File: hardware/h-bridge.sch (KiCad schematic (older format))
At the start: 46 parts, among them P3 CONN_01X02, Q3 IRFP4468, Q4 IRFP4468, Q5 IRFP4468, Q6 IRFP4468, Q7 IRFP4468, Q8 IRFP4468, U12 Si8660, U13 MIC4127, U14 LM5102, U15 LM5102

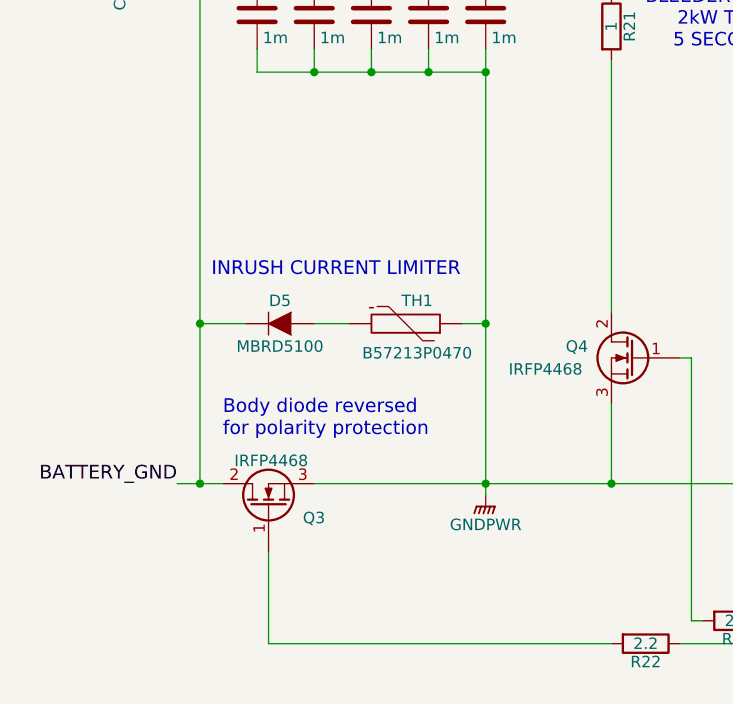
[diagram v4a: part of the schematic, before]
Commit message: Finish MCU HW draft 1; adjust sensors for 3v ref
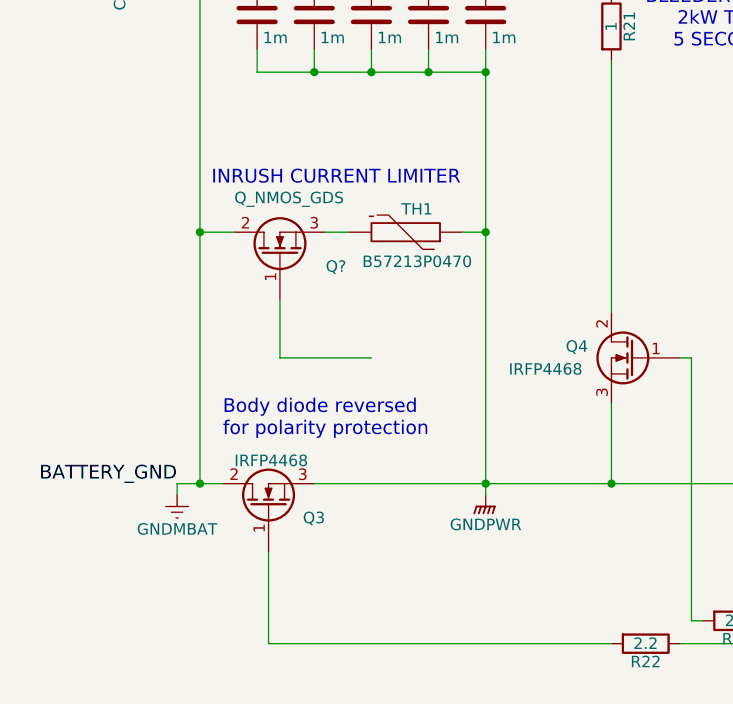
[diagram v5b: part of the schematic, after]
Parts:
- removed D5: MBRD5100, TO_SOT_Packages_SMD:TO-263-3Lead, symbol D
- added Q?: Q_NMOS_GDS, symbol Q_NMOS_GDS
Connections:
- net at TH1.2: now also Q?.3 (S)
- net BATTERY_GND renamed GNDMBAT
- net GNDMBAT: now also Q?.2 (D)
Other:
- moved on the sheet: TH1
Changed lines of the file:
@@
 L THERMISTOR TH1
 U 1 1 5986B315
-P 2550 3100
-F 0 "TH1" V 2650 3150 50  0000 C CNN
-F 1 "B57213P0470" V 2450 3150 50  0000 C BNN
-F 2 "Resistors_ThroughHole:Resistor_Vertical_RM7.5mm" H 2550 3100 50  0001 C CNN
-F 3 "" H 2550 3100 50  0000 C CNN
-	1    2550 3100
+P 2550 2700
+F 0 "TH1" V 2650 2750 50  0000 C CNN
+F 1 "B57213P0470" V 2450 2750 50  0000 C BNN
+F 2 "Resistors_ThroughHole:Resistor_Vertical_RM7.5mm" H 2550 2700 50  0001 C CNN
+F 3 "" H 2550 2700 50  0000 C CNN
+	1    2550 2700
 	0    1    -1   0
 $EndComp
@@
 Text Label 4300 6450 0    60   ~ 0
 PWM4_GD
-$Comp
-L D D5
-U 1 1 599E1390
-P 2000 3100
-F 0 "D5" H 2000 3200 50  0000 C CNN
-F 1 "MBRD5100" H 2000 3000 50  0000 C CNN
-F 2 "TO_SOT_Packages_SMD:TO-263-3Lead" H 2000 3100 50  0001 C CNN
-F 3 "" H 2000 3100 50  0000 C CNN
-	1    2000 3100
-	1    0    0    -1
-$EndComp
 Text Notes 1750 3600 0    60   ~ 0
 Body diode reversed\nfor polarity protection
@@
 	-1   0    0    -1
 $EndComp
+$Comp
+L +12V_ISO #PWR071
+U 1 1 59A0BCFD
+P 5850 4150
+F 0 "#PWR071" H 5850 4000 50  0001 C CNN
+F 1 "+12V_ISO" H 5850 4290 50  0000 C CNN
+F 2 "" H 5850 4150 50  0000 C CNN
+F 3 "" H 5850 4150 50  0000 C CNN
+	1    5850 4150
+	1    0    0    -1
+$EndComp
+$Comp
+L C_Small C42
+U 1 1 59A0C68A
+P 5850 4450
+F 0 "C42" H 5860 4520 50  0000 L CNN
+F 1 "100n" H 5860 4370 50  0000 L CNN
+F 2 "Capacitors_SMD:C_0603" H 5850 4450 50  0001 C CNN
+F 3 "" H 5850 4450 50  0000 C CNN
+	1    5850 4450
+	1    0    0    -1
+$EndComp
+Text Label 5150 4400 0    60   ~ 0
+VBUS_DIS_GD
+Text Label 5150 4500 0    60   ~ 0
+VBUS_EN_GD
+$Comp
+L R R22
+U 1 1 59A124D4
+P 3600 4500
+F 0 "R22" V 3680 4500 50  0000 C CNN
+F 1 "2.2" V 3600 4500 50  0000 C CNN
+F 2 "Resistors_SMD:R_0603" V 3530 4500 50  0001 C CNN
+F 3 "" H 3600 4500 50  0000 C CNN
+	1    3600 4500
+	0    1    1    0
+$EndComp
+$Comp
+L R R23
+U 1 1 59A12613
+P 4000 4400
+F 0 "R23" V 4080 4400 50  0000 C CNN
+F 1 "2.2" V 4000 4400 50  0000 C CNN
+F 2 "Resistors_SMD:R_0603" V 3930 4400 50  0001 C CNN
+F 3 "" H 4000 4400 50  0000 C CNN
+	1    4000 4400
+	0    1    1    0
+$EndComp
+$Comp
+L GNDPWR #PWR072
+U 1 1 59A194F2
+P 5150 3850
+F 0 "#PWR072" H 5150 3650 50  0001 C CNN
+F 1 "GNDPWR" H 5150 3720 50  0000 C CNN
+F 2 "" H 5150 3800 50  0000 C CNN
+F 3 "" H 5150 3800 50  0000 C CNN
+	1    5150 3850
+	1    0    0    -1
+$EndComp
+$Comp
+L GNDPWR #PWR073
+U 1 1 59A199E4
+P 9750 3850
+F 0 "#PWR073" H 9750 3650 50  0001 C CNN
+F 1 "GNDPWR" H 9750 3720 50  0000 C CNN
+F 2 "" H 9750 3800 50  0000 C CNN
+F 3 "" H 9750 3800 50  0000 C CNN
+	1    9750 3850
+	1    0    0    -1
+$EndComp
+$Comp
+L Si8660 U12
+U 1 1 59A1E1D2
+P 3650 6400
+F 0 "U12" H 3650 5850 60  0000 C CNN
+F 1 "Si8660" H 3650 6950 60  0000 C CNN
+F 2 "Housings_SOIC:SOIC-16_3.9x9.9mm_Pitch1.27mm" H 3650 6450 60  0001 C CNN
+F 3 "" H 3650 6450 60  0000 C CNN
+	1    3650 6400
+	1    0    0    -1
+$EndComp
+$Comp
+L GND #PWR074
+U 1 1 59A2238F
+P 3050 7000
+F 0 "#PWR074" H 3050 6750 50  0001 C CNN
+F 1 "GND" H 3050 6850 50  0000 C CNN
+F 2 "" H 3050 7000 50  0000 C CNN
+F 3 "" H 3050 7000 50  0000 C CNN
+	1    3050 7000
+	1    0    0    -1
+$EndComp
+$Comp
+L GNDPWR #PWR075
+U 1 1 59A24543
+P 4250 7100
+F 0 "#PWR075" H 4250 6900 50  0001 C CNN
+F 1 "GNDPWR" H 4250 6970 50  0000 C CNN
+F 2 "" H 4250 7050 50  0000 C CNN
+F 3 "" H 4250 7050 50  0000 C CNN
+	1    4250 7100
+	1    0    0    -1
+$EndComp
+$Comp
+L R R30
+U 1 1 59A2EED2
+P 5700 6800
+F 0 "R30" V 5780 6800 50  0000 C CNN
+F 1 "10k" V 5700 6800 50  0000 C CNN
+F 2 "Resistors_SMD:R_0603" V 5630 6800 50  0001 C CNN
+F 3 "" H 5700 6800 50  0000 C CNN
+	1    5700 6800
+	1    0    0    -1
+$EndComp
+$Comp
+L R R31
+U 1 1 59A2EED8
+P 5900 6800
+F 0 "R31" V 5980 6800 50  0000 C CNN
+F 1 "10k" V 5900 6800 50  0000 C CNN
+F 2 "Resistors_SMD:R_0603" V 5830 6800 50  0001 C CNN
+F 3 "" H 5900 6800 50  0000 C CNN
+	1    5900 6800
+	1    0    0    -1
+$EndComp
+Text Label 4300 6550 0    60   ~ 0
+VBUS_DIS_GD
+Text Label 4300 6650 0    60   ~ 0
+VBUS_EN_GD
+Text Notes 1700 2500 0    60   ~ 0
+INRUSH CURRENT LIMITER
+Text HLabel 7300 2950 3    60   BiDi ~ 0
+I_SENSE+
+Text HLabel 7550 2950 3    60   BiDi ~ 0
+I_SENSE-
+Text HLabel 8300 1450 2    60   Output ~ 0
+VBUS
+$Comp
+L GNDMBAT #PWR?
+U 1 1 59C09326
+P 1550 3850
+F 0 "#PWR?" H 1550 3600 50  0001 C CNN
+F 1 "GNDMBAT" H 1550 3700 50  0000 C CNN
+F 2 "" H 1550 3850 50  0000 C CNN
+F 3 "" H 1550 3850 50  0000 C CNN
+	1    1550 3850
+	1    0    0    -1
+$EndComp
 Wire Wire Line
 	6700 2650 6700 3300
@@
 Wire Wire Line
 	2150 1450 2150 1600
-Wire Wire Line
-	2900 1900 2900 3850
 Connection ~ 2900 2000
 Wire Wire Line
@@
 Wire Wire Line
 	1900 2000 2900 2000
-Wire Wire Line
-	2800 3100 2900 3100
-Connection ~ 2900 3100
-Wire Wire Line
-	1650 3100 1850 3100
-Connection ~ 1650 3100
+Connection ~ 1650 2700
 Connection ~ 2900 3800
 Wire Wire Line
@@
 	4900 6950 4900 7000
 Connection ~ 4900 7000
-Wire Wire Line
-	2150 3100 2300 3100
 Connection ~ 3450 3800
 Connection ~ 3450 1450
 Wire Wire Line
 	5100 4650 6050 4650
-$Comp
-L +12V_ISO #PWR071
-U 1 1 59A0BCFD
-P 5850 4150
-F 0 "#PWR071" H 5850 4000 50  0001 C CNN
-F 1 "+12V_ISO" H 5850 4290 50  0000 C CNN
-F 2 "" H 5850 4150 50  0000 C CNN
-F 3 "" H 5850 4150 50  0000 C CNN
-	1    5850 4150
-	1    0    0    -1
-$EndComp
 Wire Wire Line
 	5100 4250 5850 4250
-$Comp
-L C_Small C42
-U 1 1 59A0C68A
-P 5850 4450
-F 0 "C42" H 5860 4520 50  0000 L CNN
-F 1 "100n" H 5860 4370 50  0000 L CNN
-F 2 "Capacitors_SMD:C_0603" H 5850 4450 50  0001 C CNN
-F 3 "" H 5850 4450 50  0000 C CNN
-	1    5850 4450
-	1    0    0    -1
-$EndComp
 Wire Wire Line
 	5850 4150 5850 4350
 Wire Wire Line
 	5850 4550 5850 4650
-Text Label 5150 4400 0    60   ~ 0
-VBUS_DIS_GD
 Wire Wire Line
 	5100 4400 5150 4400
 Wire Wire Line
 	5100 4500 5150 4500
-Text Label 5150 4500 0    60   ~ 0
-VBUS_EN_GD
 Connection ~ 5850 4650
 Wire Wire Line
@@
 Wire Wire Line
 	1950 4100 1950 4500
-$Comp
-L R R22
-U 1 1 59A124D4
-P 3600 4500
-F 0 "R22" V 3680 4500 50  0000 C CNN
-F 1 "2.2" V 3600 4500 50  0000 C CNN
-F 2 "Resistors_SMD:R_0603" V 3530 4500 50  0001 C CNN
-F 3 "" H 3600 4500 50  0000 C CNN
-	1    3600 4500
-	0    1    1    0
-$EndComp
-$Comp
-L R R23
-U 1 1 59A12613
-P 4000 4400
-F 0 "R23" V 4080 4400 50  0000 C CNN
-F 1 "2.2" V 4000 4400 50  0000 C CNN
-F 2 "Resistors_SMD:R_0603" V 3930 4400 50  0001 C CNN
-F 3 "" H 4000 4400 50  0000 C CNN
-	1    4000 4400
-	0    1    1    0
-$EndComp
 Connection ~ 6050 3800
 Wire Wire Line
@@
 Wire Wire Line
 	1950 4500 3450 4500
-$Comp
-L GNDPWR #PWR072
-U 1 1 59A194F2
-P 5150 3850
-F 0 "#PWR072" H 5150 3650 50  0001 C CNN
-F 1 "GNDPWR" H 5150 3720 50  0000 C CNN
-F 2 "" H 5150 3800 50  0000 C CNN
-F 3 "" H 5150 3800 50  0000 C CNN
-	1    5150 3850
-	1    0    0    -1
-$EndComp
-$Comp
-L GNDPWR #PWR073
-U 1 1 59A199E4
-P 9750 3850
-F 0 "#PWR073" H 9750 3650 50  0001 C CNN
-F 1 "GNDPWR" H 9750 3720 50  0000 C CNN
-F 2 "" H 9750 3800 50  0000 C CNN
-F 3 "" H 9750 3800 50  0000 C CNN
-	1    9750 3850
-	1    0    0    -1
-$EndComp
 Connection ~ 5850 4250
-$Comp
-L Si8660 U12
-U 1 1 59A1E1D2
-P 3650 6400
-F 0 "U12" H 3650 5850 60  0000 C CNN
-F 1 "Si8660" H 3650 6950 60  0000 C CNN
-F 2 "Housings_SOIC:SOIC-16_3.9x9.9mm_Pitch1.27mm" H 3650 6450 60  0001 C CNN
-F 3 "" H 3650 6450 60  0000 C CNN
-	1    3650 6400
-	1    0    0    -1
-$EndComp
-$Comp
-L GND #PWR074
-U 1 1 59A2238F
-P 3050 7000
-F 0 "#PWR074" H 3050 6750 50  0001 C CNN
-F 1 "GND" H 3050 6850 50  0000 C CNN
-F 2 "" H 3050 7000 50  0000 C CNN
-F 3 "" H 3050 7000 50  0000 C CNN
-	1    3050 7000
-	1    0    0    -1
-$EndComp
-$Comp
-L GNDPWR #PWR075
-U 1 1 59A24543
-P 4250 7100
-F 0 "#PWR075" H 4250 6900 50  0001 C CNN
-F 1 "GNDPWR" H 4250 6970 50  0000 C CNN
-F 2 "" H 4250 7050 50  0000 C CNN
-F 3 "" H 4250 7050 50  0000 C CNN
-	1    4250 7100
-	1    0    0    -1
-$EndComp
 Wire Wire Line
 	3100 6850 3050 6850
@@
 Wire Wire Line
 	5300 6450 5300 6650
-$Comp
-L R R30
-U 1 1 59A2EED2
-P 5700 6800
-F 0 "R30" V 5780 6800 50  0000 C CNN
-F 1 "10k" V 5700 6800 50  0000 C CNN
-F 2 "Resistors_SMD:R_0603" V 5630 6800 50  0001 C CNN
-F 3 "" H 5700 6800 50  0000 C CNN
-	1    5700 6800
-	1    0    0    -1
-$EndComp
-$Comp
-L R R31
-U 1 1 59A2EED8
-P 5900 6800
-F 0 "R31" V 5980 6800 50  0000 C CNN
-F 1 "10k" V 5900 6800 50  0000 C CNN
-F 2 "Resistors_SMD:R_0603" V 5830 6800 50  0001 C CNN
-F 3 "" H 5900 6800 50  0000 C CNN
-	1    5900 6800
-	1    0    0    -1
-$EndComp
 Wire Wire Line
 	5700 7000 5700 6950
@@
 Wire Wire Line
 	5900 6150 5900 6650
-Text Label 4300 6550 0    60   ~ 0
-VBUS_DIS_GD
-Text Label 4300 6650 0    60   ~ 0
-VBUS_EN_GD
-Text Notes 1700 2900 0    60   ~ 0
-INRUSH CURRENT LIMITER
-Text HLabel 7300 2950 3    60   BiDi ~ 0
-I_SENSE+
-Text HLabel 7550 2950 3    60   BiDi ~ 0
-I_SENSE-
 Wire Wire Line
 	7300 2900 7300 2950
 Wire Wire Line
 	7550 2950 7550 2900
-Text HLabel 8300 1450 2    60   Output ~ 0
-VBUS
 Connection ~ 8200 1450
 Connection ~ 1900 1450
 Connection ~ 2150 1450
+Wire Wire Line
+	1550 3850 1550 3800
+Wire Wire Line
+	1650 2700 1800 2700
+Wire Wire Line
+	2200 2700 2300 2700
+Connection ~ 2900 2700
+Wire Wire Line
+	2900 2700 2800 2700
+Wire Wire Line
+	2900 1900 2900 3850
+$Comp
+L Q_NMOS_GDS Q?
+U 1 1 59C7B948
+P 2000 2800
+F 0 "Q?" V 1950 2600 50  0000 R CNN
+F 1 "Q_NMOS_GDS" V 2250 3000 50  0000 R CNN
+F 2 "" H 2200 2900 50  0000 C CNN
+F 3 "" H 2000 2800 50  0000 C CNN
+	1    2000 2800
+	0    -1   -1   0
+$EndComp
+Wire Wire Line
+	2000 3000 2000 3250
+Wire Wire Line
+	2000 3250 2400 3250
 $EndSCHEMATC

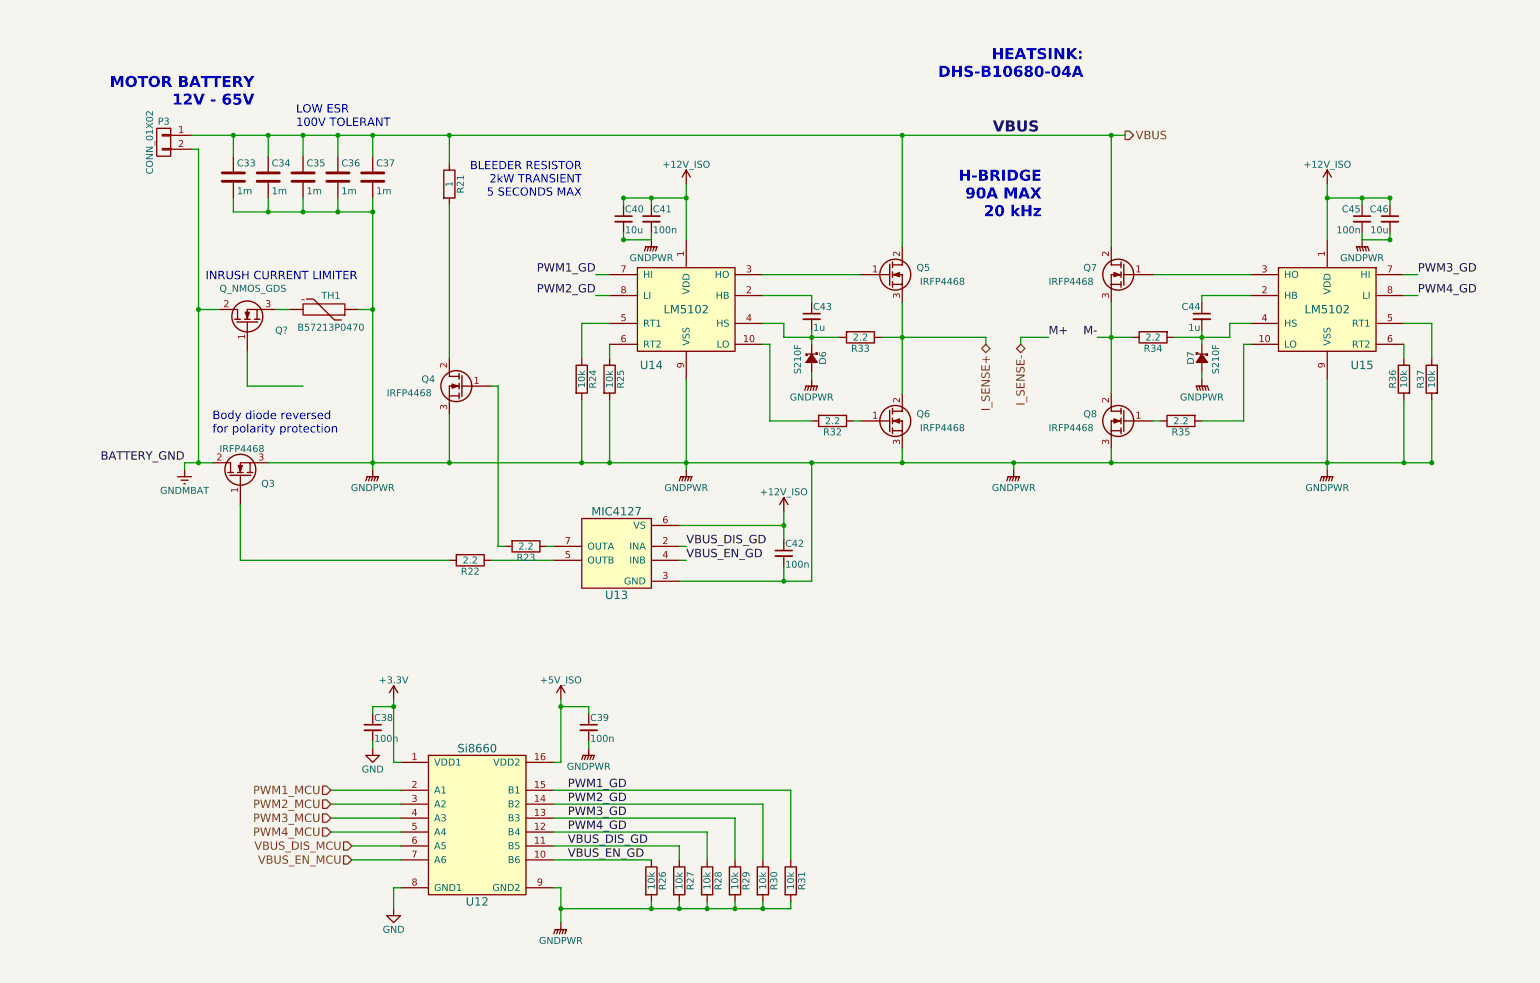
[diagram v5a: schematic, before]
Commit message: Update sensors, hbridge caps, add heatsink
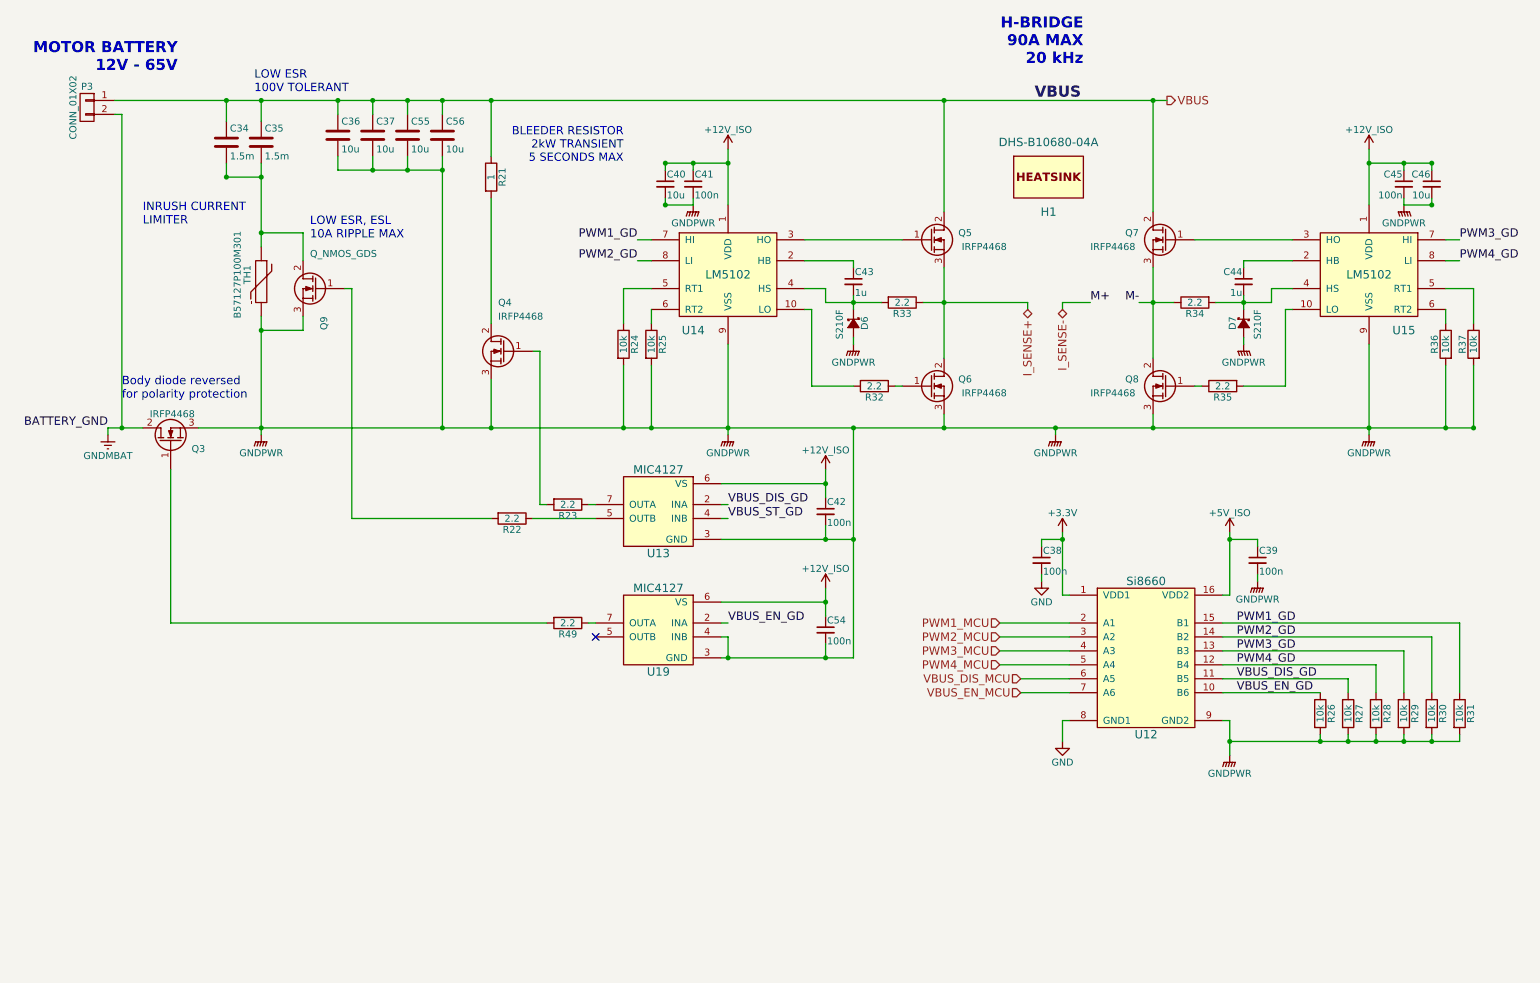
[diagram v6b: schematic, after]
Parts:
- removed C33: 1m, Capacitors_ThroughHole:C_Radial_D18_L36_P7.5, symbol C
- added C54: 100n, Capacitors_SMD:C_0603, symbol C_Small
- added C55, C56: 10u, Capacitors_SMD:C_1206, symbol C
- added H1: DHS-B10680-04A, 2kwMotorController:DHS-B10680-04A, symbol DHS-B10680-04A
- added R49: 2.2, Resistors_SMD:R_0603, symbol R
- added U19: MIC4127, symbol MIC4127
- C34, C35: value 1m -> 1.5m
- C36, C37: value 1m -> 10u; footprint Capacitors_ThroughHole:C_Radial_D18_L36_P7.5 -> Capacitors_SMD:C_1206
- TH1: value B57213P0470 -> B57127P100M301
- gave numbers to parts that had none: 1
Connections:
- net +12V_ISO: now also C54.1, U19.6 (VS)
- net GNDMBAT: no longer Q9.2 (D)
- net GNDPWR: now also Q9.3 (S), TH1.2, C54.2, C55.2, C56.2, U19.3 (GND), U19.4 (INB); no longer C34.2, C35.2, TH1.1
- net VBUS: now also C55.1, C56.1
- net VBUS_EN_GD: now also U19.2 (INA); no longer U13.4 (INB)
- net at Q3.1 (G): now also R49.2; no longer R22.2
- net at Q9.1 (G): now also R22.2
- new net: C34.2, C35.2, Q9.2 (D), TH1.1
- new net: R49.1, U19.7 (OUTA)
- new net VBUS_ST_GD: U13.4 (INB)
- no-connect marks 0 -> 1
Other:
- note added: "INRUSH CURRENT\nLIMITER"
- note added: "LOW ESR, ESL\n10A RIPPLE MAX"
- note removed: "HEATSINK:\nDHS-B10680-04A"
- note removed: "INRUSH CURRENT LIMITER"
- moved on the sheet: C34, C35, C38, C39, C40, C41, C42, C43, C44, C45, C46, D6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

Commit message: Layout first draft
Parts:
- removed U12: Si8660, Housings_SOIC:SOIC-16_3.9x9.9mm_Pitch1.27mm, symbol Si8660
- added C60, C61: 100n, Capacitors_SMD:C_0603, symbol C_Small
- added JP3, JP4: Jumper_NO_Small, Pin_Headers:Pin_Header_Straight_1x02, symbol Jumper_NO_Small
- added R53: 10k, Resistors_SMD:R_0603, symbol R
- added U12, U20: Si8640, Housings_SOIC:SOIC-16_7.5x10.3mm_Pitch1.27mm, symbol Si8640
- added W1, W2, W3, W4, W5, W6, W7: TEST_1P, symbol TEST_1P
- Q9: value Q_NMOS_GDS -> DMT10H010LK3; footprint (none) -> TO_SOT_Packages_SMD:TO-252-2Lead
- U13, U19: footprint (none) -> Housings_SOIC:SOIC-8_3.9x4.9mm_Pitch1.27mm
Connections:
- net +3V3: now also C60.1, U12.1 (VDD1), U20.1 (VDD1)
- net +5V_ISO: now also C61.1, JP3.1, JP4.1, U12.16 (VDD2), U20.16 (VDD2)
- net GND: now also C60.2, U12.2 (GND1), U12.6 (A4), U12.8 (GND1), U20.2 (GND1), U20.8 (GND1)
- net GNDPWR: now also C61.2, R53.2, U12.15 (GND2), U12.9 (GND2), U20.15 (GND2), U20.9 (GND2)
- net PWM1_GD: now also U20.14 (B1), W7.1
- net PWM1_MCU: now also U20.3 (A1)
- net PWM2_GD: now also U20.13 (B2), W6.1
- net PWM2_MCU: now also U20.4 (A2)
- net PWM3_GD: now also U20.12 (B3), W5.1
- net PWM3_MCU: now also U20.5 (A3)
- net PWM4_GD: now also U20.11 (B4), W4.1
- net PWM4_MCU: now also U20.6 (A4)
- net VBUS_DIS_GD: now also U12.13 (B2), W2.1
- net VBUS_DIS_MCU: now also U12.4 (A2)
- net VBUS_EN_GD: now also U12.12 (B3), W1.1
- net VBUS_EN_MCU: now also U12.5 (A3)
- net VBUS_ST_GD: now also R53.1, U12.14 (B1), W3.1
- net BRAKE: now reaches Q4.2 (D), R21.2
- new net: JP4.2, U20.10 (EN2)
- new net: JP3.2, U12.10 (EN2)
- new net VBUS_ST_MCU: U12.3 (A1)
- no-connect marks 1 -> 2
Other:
- moved on the sheet: C38, C39, R26, R27, R28, R29, R30, R31
